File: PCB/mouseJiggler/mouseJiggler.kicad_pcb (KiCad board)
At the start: 2 copper layers, 2 parts, among them J1 USB_A, J2 USB_A

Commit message: Updated schematic
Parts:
- added C1: 10u, Capacitor_SMD:C_0603_1608Metric, F.Cu at (133.2, 113.9)
- added C10: 10u, Capacitor_SMD:C_0603_1608Metric, F.Cu at (125.9, 121.2)
- added C11: 10u, Capacitor_SMD:C_0402_1005Metric, F.Cu at (121.3, 127.0)
- added C12: 10u, Capacitor_SMD:C_0402_1005Metric, F.Cu at (121.3, 128.9)
- added C13: 100n, Capacitor_SMD:C_0402_1005Metric, F.Cu at (124.2, 128.9)
- added C14: 30p, Capacitor_SMD:C_0402_1005Metric, F.Cu at (129.3, 119.7)
- added C15: 1u, Capacitor_SMD:C_0402_1005Metric, F.Cu at (132.3, 119.2)
- added C16: 1u, Capacitor_SMD:C_0402_1005Metric, F.Cu at (125.3, 123.4)
- added C2: 100n, Capacitor_SMD:C_0402_1005Metric, F.Cu at (129.3, 121.7)
- added C3: 1u, Capacitor_SMD:C_0402_1005Metric, F.Cu at (135.2, 118.1)
- added C4: 100n, Capacitor_SMD:C_0402_1005Metric, F.Cu at (136.6, 113.7)
- added C5: 100n, Capacitor_SMD:C_0402_1005Metric, F.Cu at (127.1, 125.6)
- added C6: 10u, Capacitor_SMD:C_0603_1608Metric, F.Cu at (128.8, 117.5)
- added C7: 30p, Capacitor_SMD:C_0402_1005Metric, F.Cu at (124.2, 127.0)
- added C8: 10u, Capacitor_SMD:C_0603_1608Metric, F.Cu at (117.9, 127.2)
- added C9: 100n, Capacitor_SMD:C_0402_1005Metric, F.Cu at (132.3, 117.2)
- added D1: LED, LED_SMD:LED_0603_1608Metric, F.Cu at (112.6, 129.6)
- added F1: 500mA, josh-passives-smt:Fuse_0603_1608Metric, F.Cu at (116.6, 129.7)
- added J3: SWD, josh-connectors:5_PIN_SMD_PROG, F.Cu at (108.4, 115.0)
- added R1: 3K3, Capacitor_SMD:C_0402_1005Metric, F.Cu at (128.2, 123.7)
- added R3: 10K, Capacitor_SMD:C_0402_1005Metric, F.Cu at (135.2, 116.2)
- added SW2: SW_Push, josh-buttons-switches:SW_PUSH_EVQPUL_EVQPUC, F.Cu at (115.2, 116.5)
- added U1: ATSAMD21E17A-M, Package_DFN_QFN:QFN-32-1EP_5x5mm_P0.5mm_EP3.6x3.6mm, F.Cu at (123.2, 116.3)
- added U2: SL2.1S, bing-SOIC:SSOP-16_4.6x2.6mm_P0.53, F.Cu at (120.6, 122.6)
- added U4: AP2112K-3.3, Package_TO_SOT_SMD:SOT-23-5, F.Cu at (113.3, 126.1)
- added Y1: 12MHz, Crystal:Crystal_SMD_2520-4Pin_2.5x2.0mm, F.Cu at (108.3, 129.5)
- moved J1 23.3 mm to (91.3, 101.2), turned to 180 degrees
- moved J2 12.1 mm to (134.6, 104.7), turned to 90 degrees
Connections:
- J1 pad 1: unconnected-(J1-Pad1) -> Net-(C10-Pad1)
- J1 pad 2: unconnected-(J1-Pad2) -> /USB_D1-
- J1 pad 3: unconnected-(J1-Pad3) -> /USB_D1+
- J1 pad 4: unconnected-(J1-Pad4) -> GND
- J1 pad 5: unconnected-(J1-Pad5) -> GND
- J2 pad 1: unconnected-(J2-Pad1) -> VBUS
- J2 pad 2: unconnected-(J2-Pad2) -> /USB_D2B-
- J2 pad 3: unconnected-(J2-Pad3) -> /USB_D2B+
- J2 pad 4: unconnected-(J2-Pad4) -> GND
- J2 pad 5: unconnected-(J2-Pad5) -> GND
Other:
- board outline added: 47.6 x 47.9 mm
- copper layers 2 -> 4

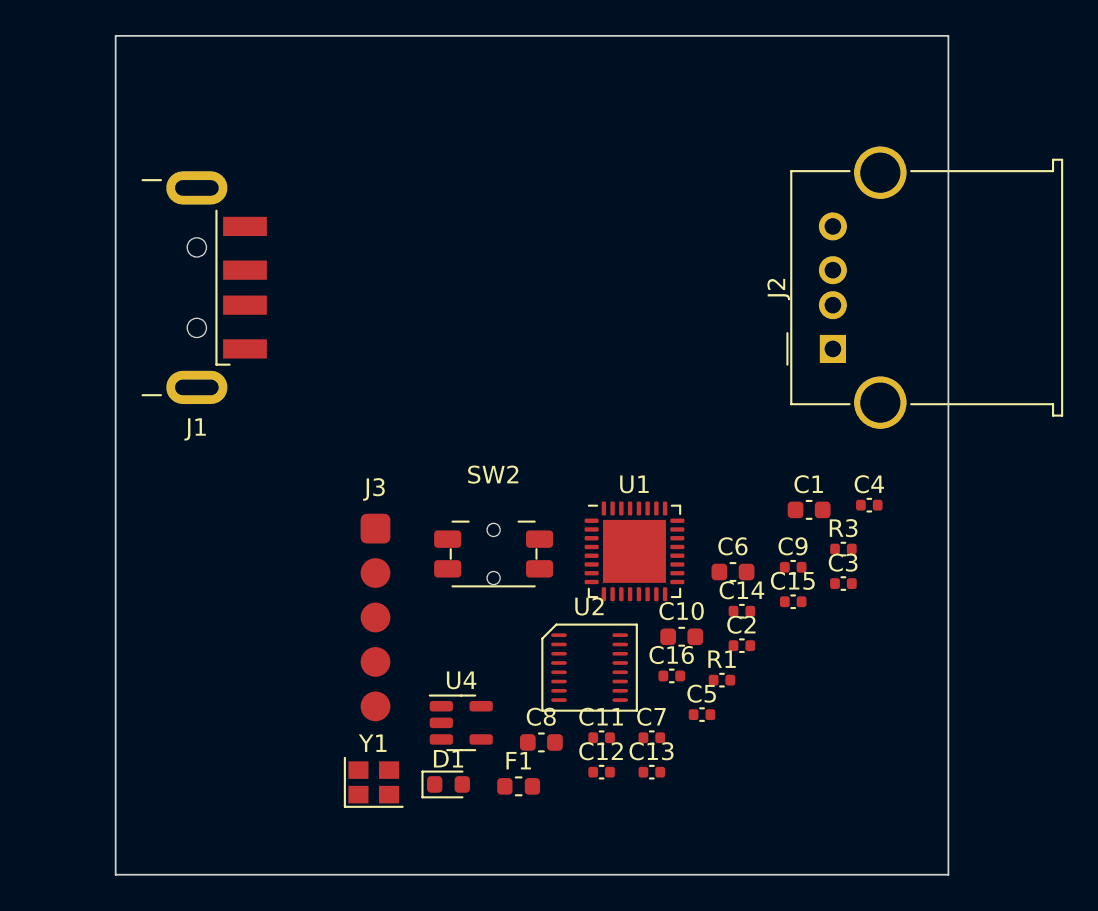
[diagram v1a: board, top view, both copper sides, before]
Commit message: Update crystal footprint
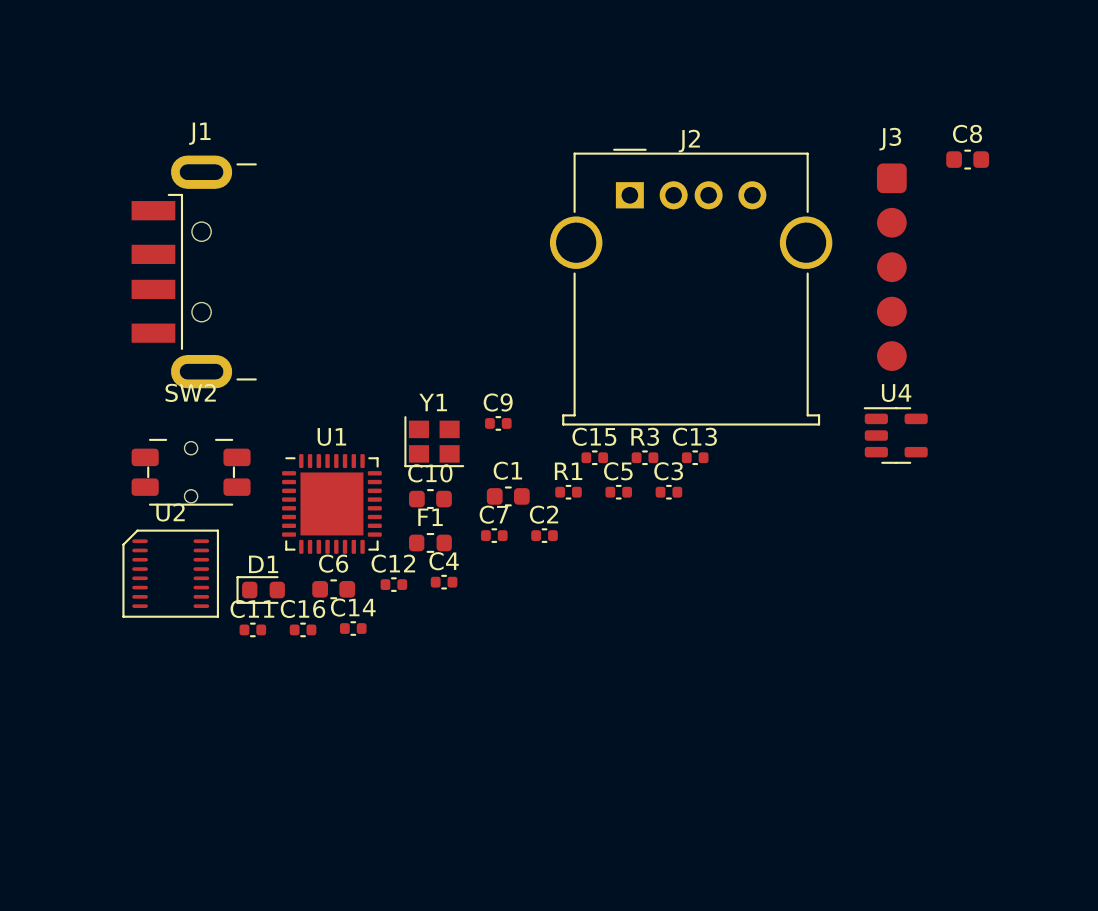
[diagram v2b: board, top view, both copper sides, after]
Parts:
- J1: footprint Connector_USB:USB_A_CNCTech_1001-011-01101_Horizontal -> bing-connector:USB_A_CNCTech_1001-011-01101_Horizontal
- J2: footprint Connector_USB:USB_A_Molex_67643_Horizontal -> bing-connector:USB_A_Molex_67643_Horizontal
- U2: footprint bing-SOIC:SSOP-16_4.6x2.6mm_P0.53 -> bing-soic:SSOP-16_4.6x2.6mm_P0.53
- Y1: footprint Crystal:Crystal_SMD_2520-4Pin_2.5x2.0mm -> bing-crystal:Crystal_SMD_2520-4Pin_2.5x2.0mm
- moved C8 41.3 mm to (142.2, 93.9)
- moved J3 35.7 mm to (137.9, 95.0)
- moved U4 29.8 mm to (138.2, 109.7)
- moved C4 24.7 mm to (112.3, 118.1)
- moved U2 24.5 mm to (96.7, 117.2)
- moved C6 22.8 mm to (106.0, 118.5)
- moved C14 22.2 mm to (107.1, 120.7)
- moved C16 21.2 mm to (104.3, 120.8)
- moved C11 20.9 mm to (101.4, 120.8)
- moved Y1 19.8 mm to (111.8, 110.0)
- moved C9 18.7 mm to (115.4, 109.0)
- moved C13 18.1 mm to (126.7, 111.0)
- moved SW2 17.9 mm to (97.9, 111.8)
- moved U1 17.5 mm to (105.9, 113.6)
- moved C1 17.2 mm to (116.0, 113.2)
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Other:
- board outline removed

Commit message: Update PCB
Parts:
- added G***: LOGO, LOGO, F.Cu at (95.5, 91.5)
- added G***: LOGO, LOGO, F.Cu at (100.7, 104.8)
- added G***: LOGO, LOGO, B.Cu at (106.1, 91.2)
- added G***: LOGO, LOGO, B.Cu at (114.5, 104.0)
- C1, C11, C12, C13, C14, C15, C16, C2, C6, C7, C8, C9, D1, J3, R1, R3, U2, U4, Y1: moved to B.Cu
- moved C8 49.0 mm to (93.4, 98.2), turned to -90 degrees
- moved J3 33.1 mm to (106.4, 104.9), turned to 90 degrees
- moved C2 30.3 mm to (96.2, 94.4), turned to 90 degrees
- moved R1 29.8 mm to (98.5, 91.7), turned to 90 degrees
- moved C1 28.4 mm to (94.9, 94.1), turned to 90 degrees
- moved U4 27.5 mm to (112.8, 99.0)
- moved D1 27.3 mm to (100.5, 91.2), turned to 180 degrees
- moved C3 26.3 mm to (104.2, 97.0), turned to -90 degrees
- moved C14 26.1 mm to (101.2, 95.3)
- moved C11 25.3 mm to (98.0, 95.7)
- moved C12 25.0 mm to (99.6, 95.2), turned to 90 degrees
- moved C4 24.3 mm to (104.5, 95.1), turned to 90 degrees
- moved C6 24.2 mm to (106.0, 94.2), turned to 90 degrees
- moved C16 24.0 mm to (115.4, 99.5), turned to 90 degrees
- moved C9 23.5 mm to (94.7, 97.9), turned to -90 degrees
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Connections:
- J2 pad 2: /USB_D2B- -> /USB_OUT-
- J2 pad 3: /USB_D2B+ -> /USB_OUT+
- U1 pad 19: /TOGGLE -> unconnected-(U1-Pad19)
- U1 pad 2: unconnected-(U1-Pad2) -> /TOGGLE
- U1 pad 23: /USB_D2A- -> /USB_JIG-
- U1 pad 24: /USB_D2A+ -> /USB_JIG+
- U2 pad 1: unconnected-(U2-Pad1) -> /USB_OUT-
- U2 pad 15: unconnected-(U2-Pad15) -> /USB_JIG-
- U2 pad 16: unconnected-(U2-Pad16) -> /USB_JIG+
- U2 pad 2: unconnected-(U2-Pad2) -> /USB_OUT+
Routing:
- net +3V3: track 0.00 -> 83.1 mm, vias 0 -> 2
- net GND: track 0.00 -> 46.0 mm, vias 0 -> 22
- net /SWD_IO: track 0.00 -> 30.6 mm, vias 0 -> 1
- net /SWD_CLK: track 0.00 -> 24.6 mm, vias 0 -> 1
- net VBUS: track 0.00 -> 15.6 mm, vias 0 -> 6
- net /nRESET: track 0.00 -> 14.8 mm, vias 0 -> 1
- net /USB_OUT+: track 0.00 -> 14.0 mm
- net /USB_OUT-: track 0.00 -> 13.2 mm
- net /TOGGLE: track 0.00 -> 9.54 mm
- net Net-(C7-Pad1): track 0.00 -> 5.83 mm
- net Net-(C10-Pad1): track 0.00 -> 4.93 mm
- net Net-(C14-Pad1): track 0.00 -> 4.72 mm
- net /USB_D1-: track 0.00 -> 4.70 mm, vias 0 -> 1
- net /USB_JIG+: track 0.00 -> 3.99 mm, vias 0 -> 1
- net /USB_D1+: track 0.00 -> 3.54 mm, vias 0 -> 1
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- added copper zone on In1.Cu, net GND
- added copper zone on In2.Cu, net VBUS
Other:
- board outline added: 27.9 x 17.6 mm
- board text added: "WFH"
- board text added: "bing"
- board text added: "opsbinxu"

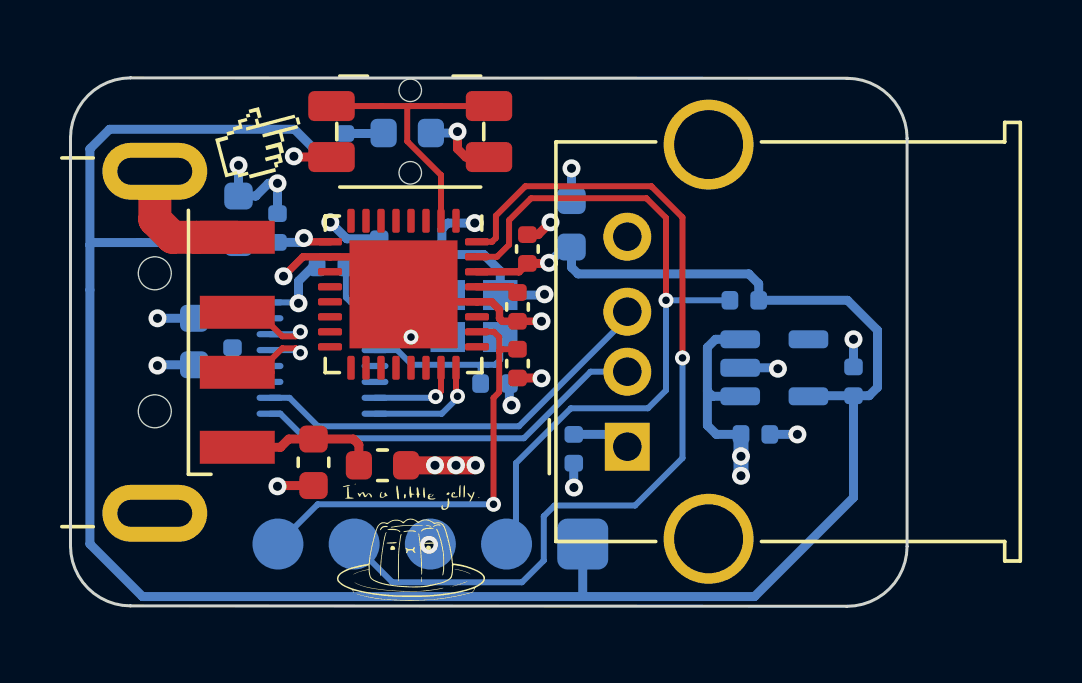
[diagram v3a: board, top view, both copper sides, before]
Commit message: Added test LED and updated PCB
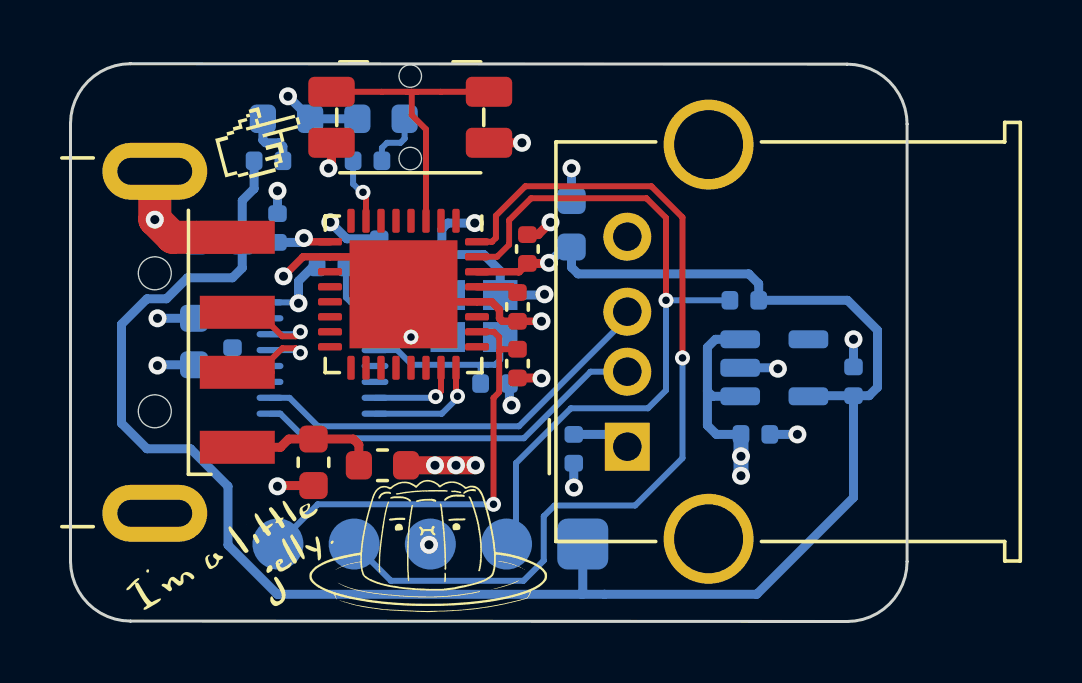
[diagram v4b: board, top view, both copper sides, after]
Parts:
- removed the G*** at (100.7, 104.8)
- added D2: LED, LED_SMD:LED_0603_1608Metric, B.Cu at (99.7, 90.8)
- added G***: LOGO, LOGO, F.Cu at (96.8, 105.5)
- added G***: LOGO, LOGO, F.Cu at (101.2, 105.0)
- added G***: LOGO, LOGO, F.Cu at (94.4, 105.1)
- added R2: 3K3, Capacitor_SMD:C_0402_1005Metric, B.Cu at (99.2, 92.2)
- moved G*** 4.72 mm to (102.5, 94.2)
- moved D1 4.05 mm to (96.5, 90.8)
- moved R1 2.59 mm to (95.9, 92.2), turned to 0 degrees
- moved C1 0.96 mm to (94.2, 94.8), turned to 180 degrees
- moved G*** 0.50 mm to (114.5, 104.5)
- moved SW2 0.47 mm to (100.6, 90.7)
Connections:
- U1 pad 2: /TOGGLE -> unconnected-(U1-Pad2)
- U1 pad 3: unconnected-(U1-Pad3) -> /TOGGLE
- U1 pad 7: unconnected-(U1-Pad7) -> /TEST
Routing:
- net +3V3: track 83.1 -> 69.1 mm
- net /TEST: track 0.00 -> 2.21 mm, vias 0 -> 1
- net Net-(D2-Pad2): track 0.00 -> 1.98 mm
- net Net-(D1-Pad2): track 1.29 -> 1.95 mm
- net GND: track 46.0 -> 45.4 mm, vias 22 -> 23
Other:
- board size 27.9 x 17.6 mm -> 27.9 x 18.6 mm
- board text added: "TEST"
- board text added: "TOGGLE"
